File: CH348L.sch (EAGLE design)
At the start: 43 parts, among them U1 AMS1117-3.3, U5 ESDU5V0H4, Y1 NX5032GA-8MHZ

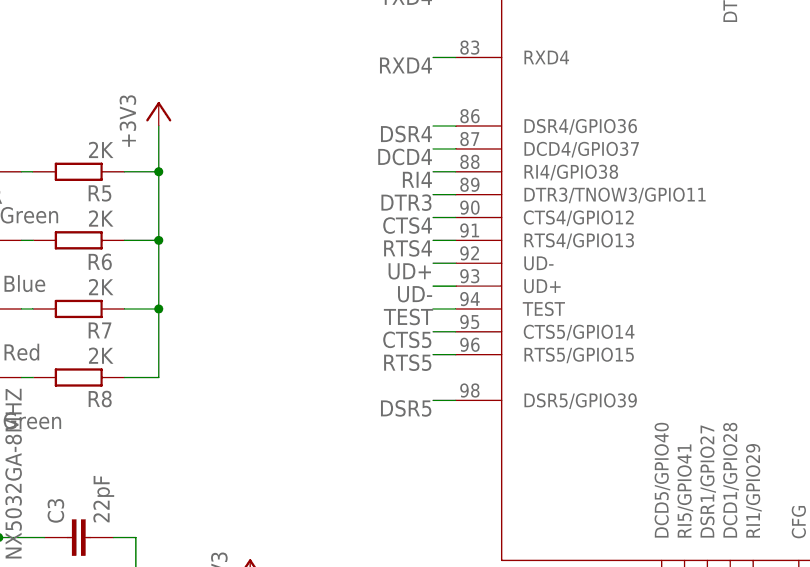
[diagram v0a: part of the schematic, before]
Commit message: Fixed UD+ UD- swap
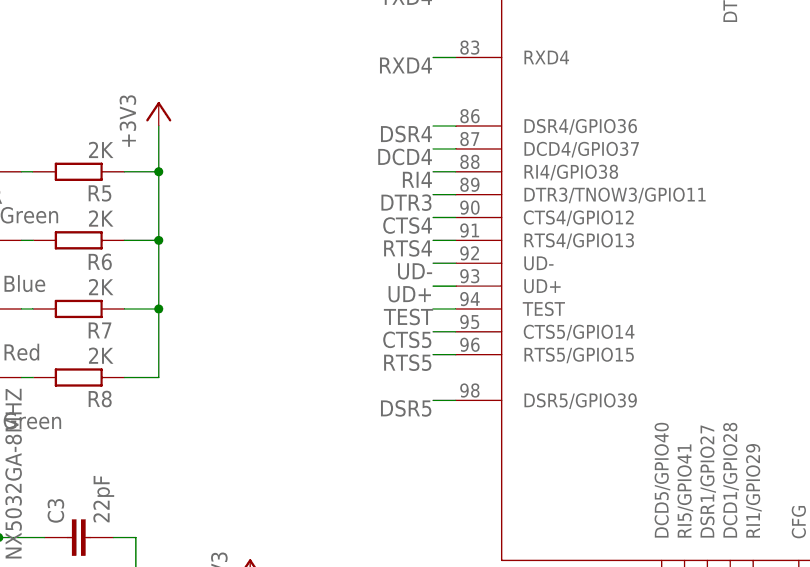
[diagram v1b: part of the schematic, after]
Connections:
- net UD+: now also U$1.UD+; no longer U$1.UD-
- net UD-: now also U$1.UD-; no longer U$1.UD+
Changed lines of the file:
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@@
 <grid distance="0.1" unitdist="inch" unit="inch" style="lines" multiple="1" display="no" altdistance="0.01" altunitdist="inch" altunit="inch"/>
 <layers>
-<layer number="1" name="Top" color="4" fill="1" visible="yes" active="no"/>
-<layer number="16" name="Bottom" color="1" fill="1" visible="yes" active="no"/>
-<layer number="17" name="Pads" color="2" fill="1" visible="yes" active="no"/>
-<layer number="18" name="Vias" color="2" fill="1" visible="yes" active="no"/>
-<layer number="19" name="Unrouted" color="6" fill="1" visible="yes" active="no"/>
-<layer number="20" name="Dimension" color="24" fill="1" visible="yes" active="no"/>
-<layer number="21" name="tPlace" color="7" fill="1" visible="yes" active="no"/>
-<layer number="22" name="bPlace" color="7" fill="1" visible="yes" active="no"/>
-<layer number="23" name="tOrigins" color="15" fill="1" visible="yes" active="no"/>
-<layer number="24" name="bOrigins" color="15" fill="1" visible="yes" active="no"/>
-<layer number="25" name="tNames" color="7" fill="1" visible="yes" active="no"/>
-<layer number="26" name="bNames" color="7" fill="1" visible="yes" active="no"/>
-<layer number="27" name="tValues" color="7" fill="1" visible="yes" active="no"/>
-<layer number="28" name="bValues" color="7" fill="1" visible="yes" active="no"/>
+<layer number="1" name="Top" color="4" fill="1" visible="no" active="no"/>
+<layer number="16" name="Bottom" color="1" fill="1" visible="no" active="no"/>
+<layer number="17" name="Pads" color="2" fill="1" visible="no" active="no"/>
+<layer number="18" name="Vias" color="2" fill="1" visible="no" active="no"/>
+<layer number="19" name="Unrouted" color="6" fill="1" visible="no" active="no"/>
+<layer number="20" name="Dimension" color="24" fill="1" visible="no" active="no"/>
+<layer number="21" name="tPlace" color="7" fill="1" visible="no" active="no"/>
+<layer number="22" name="bPlace" color="7" fill="1" visible="no" active="no"/>
+<layer number="23" name="tOrigins" color="15" fill="1" visible="no" active="no"/>
+<layer number="24" name="bOrigins" color="15" fill="1" visible="no" active="no"/>
+<layer number="25" name="tNames" color="7" fill="1" visible="no" active="no"/>
+<layer number="26" name="bNames" color="7" fill="1" visible="no" active="no"/>
+<layer number="27" name="tValues" color="7" fill="1" visible="no" active="no"/>
+<layer number="28" name="bValues" color="7" fill="1" visible="no" active="no"/>
 <layer number="29" name="tStop" color="7" fill="3" visible="no" active="no"/>
 <layer number="30" name="bStop" color="7" fill="6" visible="no" active="no"/>
@@
 <layer number="35" name="tGlue" color="7" fill="4" visible="no" active="no"/>
 <layer number="36" name="bGlue" color="7" fill="5" visible="no" active="no"/>
-<layer number="37" name="tTest" color="7" fill="1" visible="yes" active="no"/>
-<layer number="38" name="bTest" color="7" fill="1" visible="yes" active="no"/>
+<layer number="37" name="tTest" color="7" fill="1" visible="no" active="no"/>
+<layer number="38" name="bTest" color="7" fill="1" visible="no" active="no"/>
 <layer number="39" name="tKeepout" color="4" fill="11" visible="no" active="no"/>
 <layer number="40" name="bKeepout" color="1" fill="11" visible="no" active="no"/>
@@
 <layer number="44" name="Drills" color="7" fill="1" visible="no" active="no"/>
 <layer number="45" name="Holes" color="7" fill="1" visible="no" active="no"/>
-<layer number="46" name="Milling" color="3" fill="1" visible="yes" active="no"/>
-<layer number="47" name="Measures" color="7" fill="1" visible="yes" active="no"/>
-<layer number="48" name="Document" color="7" fill="1" visible="yes" active="no"/>
-<layer number="49" name="Reference" color="7" fill="1" visible="yes" active="no"/>
-<layer number="50" name="dxf" color="7" fill="1" visible="yes" active="no"/>
-<layer number="51" name="tDocu" color="7" fill="1" visible="yes" active="no"/>
-<layer number="52" name="bDocu" color="7" fill="1" visible="yes" active="no"/>
-<layer number="53" name="tGND_GNDA" color="7" fill="9" visible="yes" active="no"/>
-<layer number="54" name="bGND_GNDA" color="1" fill="9" visible="yes" active="no"/>
-<layer number="56" name="wert" color="7" fill="1" visible="yes" active="no"/>
-<layer number="57" name="tCAD" color="7" fill="1" visible="yes" active="no"/>
-<layer number="58" name="b3D" color="7" fill="1" visible="yes" active="no"/>
-<layer number="59" name="tCarbon" color="7" fill="1" visible="yes" active="no"/>
-<layer number="60" name="bCarbon" color="7" fill="1" visible="yes" active="no"/>
+<layer number="46" name="Milling" color="3" fill="1" visible="no" active="no"/>
+<layer number="47" name="Measures" color="7" fill="1" visible="no" active="no"/>
+<layer number="48" name="Document" color="7" fill="1" visible="no" active="no"/>
+<layer number="49" name="Reference" color="7" fill="1" visible="no" active="no"/>
+<layer number="50" name="dxf" color="7" fill="1" visible="no" active="no"/>
+<layer number="51" name="tDocu" color="7" fill="1" visible="no" active="no"/>
+<layer number="52" name="bDocu" color="7" fill="1" visible="no" active="no"/>
+<layer number="53" name="tGND_GNDA" color="7" fill="9" visible="no" active="no"/>
+<layer number="54" name="bGND_GNDA" color="1" fill="9" visible="no" active="no"/>
+<layer number="56" name="wert" color="7" fill="1" visible="no" active="no"/>
+<layer number="57" name="tCAD" color="7" fill="1" visible="no" active="no"/>
+<layer number="58" name="b3D" color="7" fill="1" visible="no" active="no"/>
+<layer number="59" name="tCarbon" color="7" fill="1" visible="no" active="no"/>
+<layer number="60" name="bCarbon" color="7" fill="1" visible="no" active="no"/>
 <layer number="88" name="SimResults" color="9" fill="1" visible="yes" active="yes"/>
 <layer number="89" name="SimProbes" color="9" fill="1" visible="yes" active="yes"/>
@@
 </segment>
 <segment>
+<pinref part="U$1" gate="G$1" pin="UD+"/>
+<wire x1="-50.8" y1="-12.7" x2="-53.34" y2="-12.7" width="0.1524" layer="91"/>
+<label x="-53.34" y="-12.7" size="1.778" layer="95" rot="R180"/>
+</segment>
+</net>
+<net name="UD-" class="0">
+<segment>
+<pinref part="USBC" gate="G$1" pin="DN1"/>
+<wire x1="-93.98" y1="78.74" x2="-96.52" y2="78.74" width="0.1524" layer="91"/>
+<label x="-96.52" y="78.74" size="1.778" layer="95" rot="R180"/>
+</segment>
+<segment>
+<pinref part="USBC" gate="G$1" pin="DN2"/>
+<wire x1="-58.42" y1="81.28" x2="-55.88" y2="81.28" width="0.1524" layer="91"/>
+<label x="-55.88" y="81.28" size="1.778" layer="95"/>
+</segment>
+<segment>
+<pinref part="U5" gate="G$1" pin="IO2"/>
+<wire x1="-15.24" y1="73.66" x2="-12.7" y2="73.66" width="0.1524" layer="91"/>
+<label x="-12.7" y="73.66" size="1.778" layer="95"/>
+</segment>
+<segment>
 <pinref part="U$1" gate="G$1" pin="UD-"/>
 <wire x1="-50.8" y1="-10.16" x2="-53.34" y2="-10.16" width="0.1524" layer="91"/>
@@
 </segment>
 </net>
-<net name="UD-" class="0">
-<segment>
-<pinref part="USBC" gate="G$1" pin="DN1"/>
-<wire x1="-93.98" y1="78.74" x2="-96.52" y2="78.74" width="0.1524" layer="91"/>
-<label x="-96.52" y="78.74" size="1.778" layer="95" rot="R180"/>
-</segment>
-<segment>
-<pinref part="USBC" gate="G$1" pin="DN2"/>
-<wire x1="-58.42" y1="81.28" x2="-55.88" y2="81.28" width="0.1524" layer="91"/>
-<label x="-55.88" y="81.28" size="1.778" layer="95"/>
-</segment>
-<segment>
-<pinref part="U5" gate="G$1" pin="IO2"/>
-<wire x1="-15.24" y1="73.66" x2="-12.7" y2="73.66" width="0.1524" layer="91"/>
-<label x="-12.7" y="73.66" size="1.778" layer="95"/>
-</segment>
-<segment>
-<pinref part="U$1" gate="G$1" pin="UD+"/>
-<wire x1="-50.8" y1="-12.7" x2="-53.34" y2="-12.7" width="0.1524" layer="91"/>
-<label x="-53.34" y="-12.7" size="1.778" layer="95" rot="R180"/>
-</segment>
-</net>
